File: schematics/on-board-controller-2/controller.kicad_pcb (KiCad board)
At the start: 2 copper layers, 90 x 60 mm, 75 parts, among them J1 5-1814832-1, J2 programmer, J3 xt60, M1 Motor_DC, M2 Motor_DC, M3 Stepper_Motor_bipolar, Q1 NMOS, U1 L293D, U2 STM32L476RGTx, U3 L293D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

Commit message: updates
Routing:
- net GND: vias 237 -> 239
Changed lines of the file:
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@@
 		(tags "THT Terminal Block Xinya XY308-2.54-2P pitch 2.54mm size 5.58x6.5mm^2 drill 1.2mm pad 2mm")
 		(property "Reference" "M2"
-			(at 3.085 -3.595 -90)
+			(at -0.915 5.155 -90)
 			(layer "F.SilkS")
 			(effects
@@
 	)
 	(via
+		(at 147 115)
+		(size 0.6)
+		(drill 0.3)
+		(layers "F.Cu" "B.Cu")
+		(free yes)
+		(net 2)
+	)
+	(via
 		(at 72 77.5)
 		(size 0.6)
@@
 	)
 	(via
-		(at 136.25 117.75)
+		(at 135 116)
 		(size 0.6)
 		(drill 0.3)
@@
 	)
 	(via
+		(at 135 78)
+		(size 0.6)
+		(drill 0.3)
+		(layers "F.Cu" "B.Cu")
+		(free yes)
+		(net 2)
+	)
+	(via
 		(at 72.25 107.75)
 		(size 0.6)
@@
 	)
 	(via
-		(at 149.25 117.75)
+		(at 150 118)
 		(size 0.6)
 		(drill 0.3)

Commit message: changed footprint for electrolytic capacitors
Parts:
- C19, C20, C4: footprint Capacitor_THT:CP_Radial_D5.0mm_P2.50mm -> Capacitor_THT:CP_Radial_D5.0mm_P2.00mm

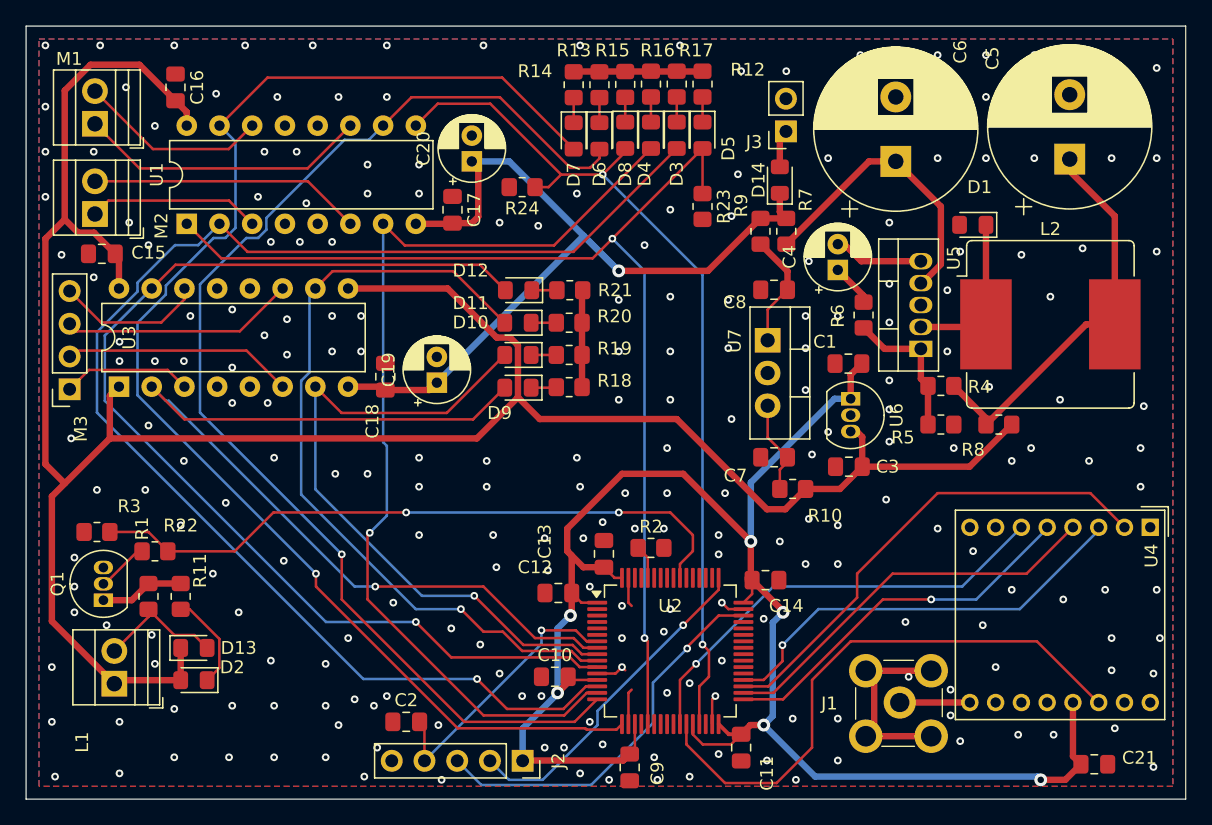
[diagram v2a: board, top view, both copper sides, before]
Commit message: added a bom and edited layout
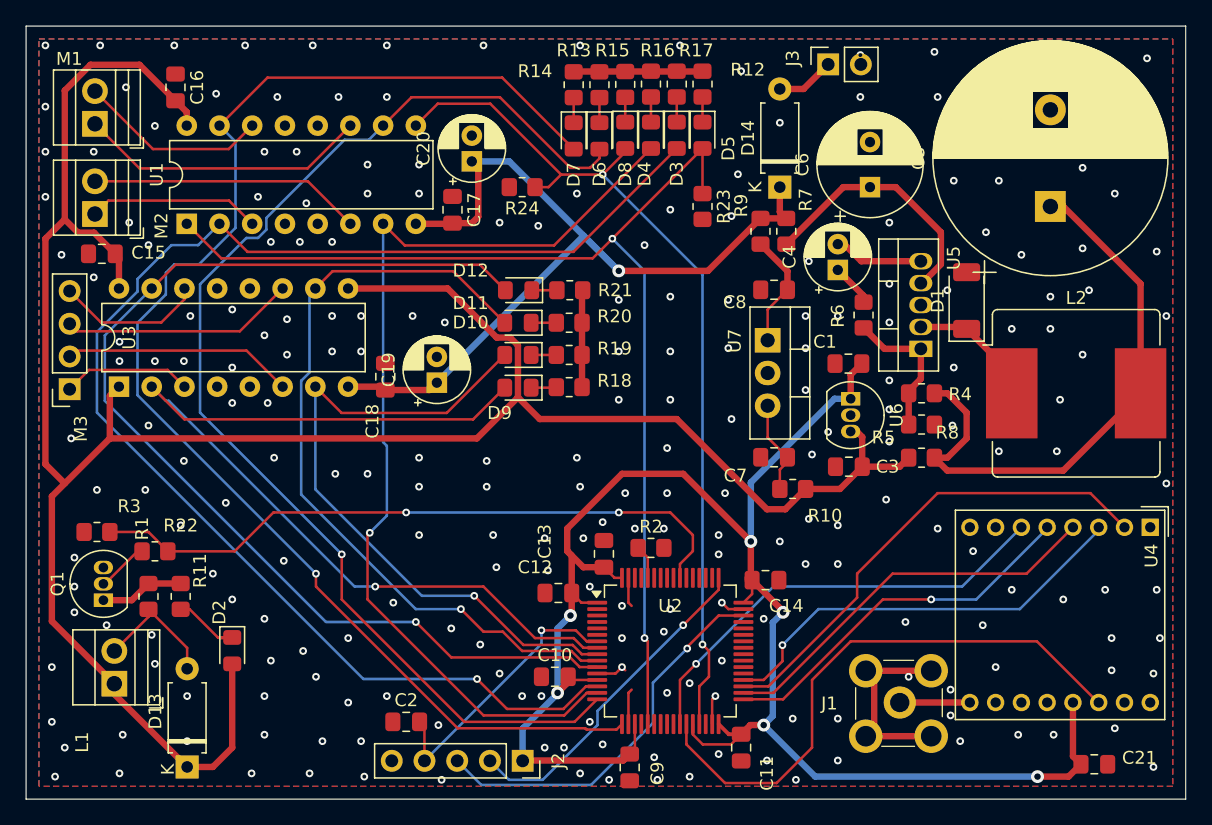
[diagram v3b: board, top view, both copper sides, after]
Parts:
- C5: footprint Capacitor_THT:CP_Radial_D12.5mm_P5.00mm -> Capacitor_THT:CP_Radial_D18.0mm_P7.50mm
- C6: footprint Capacitor_THT:CP_Radial_D12.5mm_P5.00mm -> Capacitor_THT:CP_Radial_D8.0mm_P3.50mm
- D1: footprint Diode_SMD:D_0805_2012Metric_Pad1.15x1.40mm_HandSolder -> Diode_SMD:D_SOD-128
- D13, D14: footprint LED_SMD:LED_0805_2012Metric_Pad1.15x1.40mm_HandSolder -> Diode_THT:D_A-405_P7.62mm_Horizontal
- moved D13 9.25 mm to (75.0, 118.0), turned to 90 degrees
- moved R8 6.53 mm to (132.0, 94.0), turned to 180 degrees
- moved J3 6.15 mm to (124.8, 63.5), turned to 90 degrees
- moved D1 5.89 mm to (135.5, 81.8), turned to 90 degrees
- moved L2 5.71 mm to (144.0, 89.0)
- moved C5 3.97 mm to (142.0, 74.5)
- moved D2 3.75 mm to (78.5, 109.0), turned to -90 degrees
- moved C6 2.83 mm to (128.0, 73.0)
- moved R4 1.61 mm to (132.0, 89.0)
- moved R5 1.50 mm to (132.0, 91.4)
- moved D14 0.55 mm to (121.0, 73.0)
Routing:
- net Net-(C5-Pad1): track 32.0 -> 45.1 mm
- net Net-(D1-K): track 13.6 -> 10.3 mm
- net Net-(U5-INPUT): track 22.8 -> 19.9 mm
- net +6V: track 188.3 -> 190.9 mm
- net Net-(D2-K): track 7.55 -> 5.93 mm
- net Net-(D14-A): track 2.95 -> 4.54 mm
- net DC_MOTOR4: track 105.6 -> 106.1 mm
- net GND: vias 239 -> 245

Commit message: submitted version for checking
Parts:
- moved R8 1.00 mm to (132.0, 95.0)
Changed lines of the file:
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@@
 		(tags "resistor handsolder")
 		(property "Reference" "R5"
-			(at -2.952271 1 0)
+			(at -2.5 2.073959 0)
 			(layer "F.SilkS")
 			(effects
@@
 	(footprint "Resistor_SMD:R_0805_2012Metric_Pad1.20x1.40mm_HandSolder"
 		(layer "F.Cu")
-		(at 132 94 180)
+		(at 132 95 180)
 		(descr "Resistor SMD 0805 (2012 Metric), square (rectangular) end terminal, IPC_7351 nominal with elongated pad for handsoldering. (Body size source: IPC-SM-782 page 72, https://www.pcb-3d.com/wordpress/wp-content/uploads/ipc-sm-782a_amendment_1_and_2.pdf), generated with kicad-footprint-generator")
 		(tags "resistor handsolder")
 		(property "Reference" "R8"
-			(at -2 1.952271 360)
+			(at -2 1.952271 0)
 			(layer "F.SilkS")
 			(effects
@@
 		)
 		(property "Value" "0"
-			(at 0 1.65 360)
+			(at 0 1.65 0)
 			(layer "F.Fab")
 			(effects
@@
 		)
 		(fp_text user "${REFERENCE}"
-			(at 0 0 360)
+			(at 0 0 0)
 			(layer "F.Fab")
 			(effects
@@
 		(tags "CP Radial series Radial pin pitch 2.00mm  diameter 5mm Electrolytic Capacitor")
 		(property "Reference" "C4"
-			(at 1 -3.75 90)
+			(at -2.573959 -1 180)
 			(layer "F.SilkS")
 			(effects
@@
 		)
 		(fp_text user "${REFERENCE}"
-			(at 0 1.27 360)
+			(at 0 1.27 0)
 			(layer "F.Fab")
 			(effects
@@
 		(tags "TO-220-5 Vertical RM 1.7mm Pentawatt Multiwatt-5")
 		(property "Reference" "U5"
-			(at 7.049811 2.555 90)
+			(at -0.950189 2.555 90)
 			(layer "F.SilkS")
 			(effects
@@
 		(tags "CP Radial series Radial pin pitch 3.50mm  diameter 8mm Electrolytic Capacitor")
 		(property "Reference" "C6"
-			(at 1.75 -5.25 90)
+			(at 6 -3.5 90)
 			(layer "F.SilkS")
 			(effects
@@
 		(tags "CP Radial series Radial pin pitch 2.00mm  diameter 5mm Electrolytic Capacitor")
 		(property "Reference" "C19"
-			(at 1 -3.75 90)
+			(at 4.174657 -1.88 180)
 			(layer "F.SilkS")
 			(effects
@@
 		(tags "to-92 sc-43 sc-43a sot54 PA33 transistor")
 		(property "Reference" "U6"
-			(at 1.27 -3.56 90)
+			(at -0.926041 -3 90)
 			(layer "F.SilkS")
 			(effects
@@
 		(tags "Diode A-405 series Axial Horizontal pin pitch 7.62mm  length 5.2mm diameter 2.7mm")
 		(property "Reference" "D13"
-			(at 4.31 -2.47 90)
+			(at 4.31 2.5 90)
 			(layer "F.SilkS")
 			(effects
@@
 		(tags "D_SOD-128")
 		(property "Reference" "D1"
-			(at 0 -2.25 90)
+			(at 0.8 3 180)
 			(layer "F.SilkS")
 			(effects
@@
 		(tags "CP Radial series Radial pin pitch 7.50mm  diameter 18mm Electrolytic Capacitor")
 		(property "Reference" "C5"
-			(at 3.75 -10.25 90)
+			(at 7 -10 90)
 			(layer "F.SilkS")
 			(effects
@@
 		(tags "resistor handsolder")
 		(property "Reference" "R6"
-			(at 0.073959 2 90)
+			(at 0.573959 2 90)
 			(layer "F.SilkS")
 			(effects
@@
 		(tags "CP Radial series Radial pin pitch 2.00mm  diameter 5mm Electrolytic Capacitor")
 		(property "Reference" "C20"
-			(at 1 -3.75 90)
+			(at 4.500113 -0.095 180)
 			(layer "F.SilkS")
 			(effects
@@
 	)
 	(via
-		(at 127.25 62.75)
+		(at 121.5 62.5)
 		(size 0.6)
 		(drill 0.3)
@@
 	)
 	(segment
-		(start 127.3975 94.696041)
-		(end 130.303959 94.696041)
-		(width 0.5)
-		(layer "F.Cu")
-		(net 71)
-	)
-	(segment
 		(start 71.3 63.5)
 		(end 67.5 63.5)
@@
 	)
 	(segment
-		(start 130.303959 94.696041)
-		(end 131 94)
-		(width 0.5)
-		(layer "F.Cu")
-		(net 71)
-	)
-	(segment
 		(start 69.35 112.35)
 		(end 75 118)
@@
 	)
 	(segment
+		(start 127.3975 94.696041)
+		(end 130.696041 94.696041)
+		(width 0.5)
+		(layer "F.Cu")
+		(net 71)
+	)
+	(segment
 		(start 65.5 75.5)
 		(end 64 77)
@@
 	)
 	(segment
+		(start 130.696041 94.696041)
+		(end 131 95)
+		(width 0.5)
+		(layer "F.Cu")
+		(net 71)
+	)
+	(segment
 		(start 69.71 80.865)
 		(end 69.71 78.467157)
@@
 	(segment
 		(start 135.5 92.5)
-		(end 135.5 90.5)
+		(end 133 95)
 		(width 0.5)
 		(layer "F.Cu")
@@
 	)
 	(segment
-		(start 133 94)
-		(end 134 95)
-		(width 0.5)
-		(layer "F.Cu")
-		(net 74)
-	)
-	(segment
-		(start 149 80.5)
+		(start 143 95)
 		(end 149 89)
 		(width 0.5)
@@
 	)
 	(segment
-		(start 133 94)
-		(end 134 94)
-		(width 0.5)
-		(layer "F.Cu")
-		(net 74)
-	)
-	(segment
-		(start 143 95)
+		(start 149 80.5)
 		(end 149 89)
 		(width 0.5)
@@
 	)
 	(segment
-		(start 134 95)
-		(end 143 95)
+		(start 142 74.5)
+		(end 143 74.5)
 		(width 0.5)
 		(layer "F.Cu")
@@
 	)
 	(segment
-		(start 142 74.5)
-		(end 143 74.5)
+		(start 133 89)
+		(end 134 89)
 		(width 0.5)
 		(layer "F.Cu")
@@
 	)
 	(segment
-		(start 134 94)
+		(start 135.5 90.5)
 		(end 135.5 92.5)
 		(width 0.5)
@@
 	)
 	(segment
-		(start 135.5 90.5)
-		(end 134 89)
+		(start 133 95)
+		(end 143 95)
 		(width 0.5)
 		(layer "F.Cu")
@@
 	(segment
 		(start 134 89)
-		(end 133 89)
+		(end 135.5 90.5)
 		(width 0.5)
 		(layer "F.Cu")
